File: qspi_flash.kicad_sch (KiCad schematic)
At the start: 5 parts, among them SW1 BOOTSEL, U2 W25Q128JVS

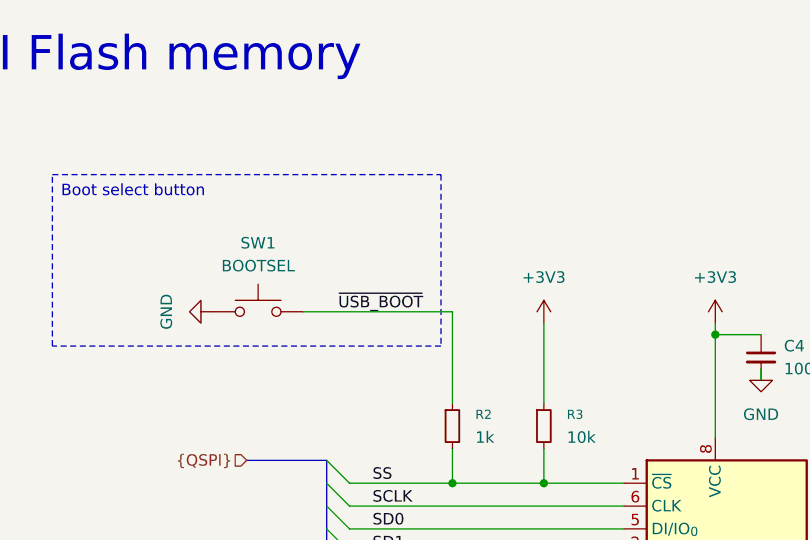
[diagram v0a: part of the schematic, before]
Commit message: spostato hardware in the loop  a connettore fpc e fixata etichetta bootsel
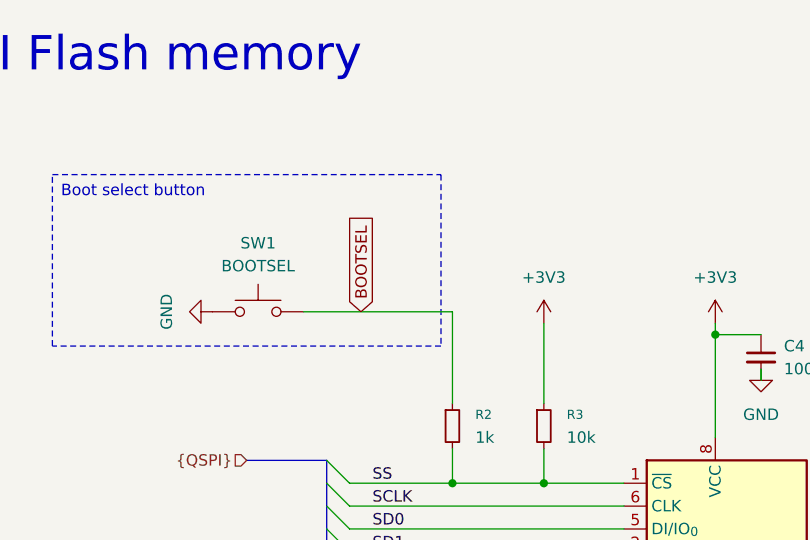
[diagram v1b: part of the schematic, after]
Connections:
- net ~{USB_BOOT} renamed BOOTSEL
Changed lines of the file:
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@@
-		)
-	)
-	(label "~{USB_BOOT}"
-		(at 66.04 46.99 0)
-		(effects
-			(font
-				(size 1.27 1.27)
-			)
-			(justify left bottom)
 		)
 	)
@@
 		)
 	)
+	(global_label "BOOTSEL"
+		(shape input)
+		(at 68.58 46.99 90)
+		(fields_autoplaced yes)
+		(effects
+			(font
+				(size 1.27 1.27)
+			)
+			(justify left)
+		)
+		(property "Intersheetrefs" "${INTERSHEET_REFS}"
+			(at 68.58 35.7196 90)
+			(effects
+				(font
+					(size 1.27 1.27)
+				)
+				(justify left)
+				(hide yes)
+			)
+		)
+	)
